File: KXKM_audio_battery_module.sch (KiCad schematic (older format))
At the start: 22 parts, among them J1 Conn_01x06, J2 TEST_1P, J3 mikroBUS_socket, J4 Conn_01x04, J5 Micro_SD_Card, J6 Conn_01x03, J7 Conn_01x04, Q1 DMN63D8LDW, Q2 DMN63D8LDW, SW1 SW_Push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

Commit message: Component placement WIP - multiple Hammond enclosures drawn
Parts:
- RN1, RN2, RN3: footprint (none) -> Resistors_SMD:R_Array_Convex_4x0402
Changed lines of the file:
@@
 F 0 "RN1" H 2130 4470 50  0000 L CNN
 F 1 "10k" H 2130 4410 50  0000 L CNN
-F 2 "" H 2100 4450 50  0001 C CNN
+F 2 "Resistors_SMD:R_Array_Convex_4x0402" H 2100 4450 50  0001 C CNN
 F 3 "" H 2100 4450 50  0001 C CNN
 	3    2100 4450
@@
 F 0 "RN1" H 2030 4470 50  0000 L CNN
 F 1 "10k" H 2030 4410 50  0000 L CNN
-F 2 "" H 2000 4450 50  0001 C CNN
+F 2 "Resistors_SMD:R_Array_Convex_4x0402" H 2000 4450 50  0001 C CNN
 F 3 "" H 2000 4450 50  0001 C CNN
 	2    2000 4450
@@
 F 0 "RN1" H 3480 1870 50  0000 L CNN
 F 1 "10k" H 3480 1810 50  0000 L CNN
-F 2 "" H 3450 1850 50  0001 C CNN
+F 2 "Resistors_SMD:R_Array_Convex_4x0402" H 3450 1850 50  0001 C CNN
 F 3 "" H 3450 1850 50  0001 C CNN
 	4    3450 1850
@@
 F 0 "RN3" H 9830 5220 50  0000 L CNN
 F 1 "10k" H 9830 5160 50  0000 L CNN
-F 2 "" H 9800 5200 50  0001 C CNN
+F 2 "Resistors_SMD:R_Array_Convex_4x0402" H 9800 5200 50  0001 C CNN
 F 3 "" H 9800 5200 50  0001 C CNN
 	1    9800 5200
@@
 F 0 "RN3" H 9830 5870 50  0000 L CNN
 F 1 "10k" H 9830 5810 50  0000 L CNN
-F 2 "" H 9800 5850 50  0001 C CNN
+F 2 "Resistors_SMD:R_Array_Convex_4x0402" H 9800 5850 50  0001 C CNN
 F 3 "" H 9800 5850 50  0001 C CNN
 	2    9800 5850
@@
 F 0 "RN2" H 8930 5870 50  0000 L CNN
 F 1 "10k" H 8930 5810 50  0000 L CNN
-F 2 "" H 8900 5850 50  0001 C CNN
+F 2 "Resistors_SMD:R_Array_Convex_4x0402" H 8900 5850 50  0001 C CNN
 F 3 "" H 8900 5850 50  0001 C CNN
 	4    8900 5850
@@
 F 0 "RN2" H 8930 5220 50  0000 L CNN
 F 1 "10k" H 8930 5160 50  0000 L CNN
-F 2 "" H 8900 5200 50  0001 C CNN
+F 2 "Resistors_SMD:R_Array_Convex_4x0402" H 8900 5200 50  0001 C CNN
 F 3 "" H 8900 5200 50  0001 C CNN
 	3    8900 5200
@@
 F 0 "RN1" V 1850 6850 50  0000 L CNN
 F 1 "10k" V 1850 7150 50  0000 L CNN
-F 2 "" H 1900 7050 50  0001 C CNN
+F 2 "Resistors_SMD:R_Array_Convex_4x0402" H 1900 7050 50  0001 C CNN
 F 3 "" H 1900 7050 50  0001 C CNN
 	1    1900 7050
@@
 F 0 "RN2" V 3450 7150 50  0000 L CNN
 F 1 "10k" V 3650 7150 50  0000 L CNN
-F 2 "" H 3550 7250 50  0001 C CNN
+F 2 "Resistors_SMD:R_Array_Convex_4x0402" H 3550 7250 50  0001 C CNN
 F 3 "" H 3550 7250 50  0001 C CNN
 	2    3550 7250
@@
 F 0 "RN2" V 3450 6650 50  0000 L CNN
 F 1 "10k" V 3650 6650 50  0000 L CNN
-F 2 "" H 3550 6750 50  0001 C CNN
+F 2 "Resistors_SMD:R_Array_Convex_4x0402" H 3550 6750 50  0001 C CNN
 F 3 "" H 3550 6750 50  0001 C CNN
 	1    3550 6750

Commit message: Almost all components placed... Saving before mirroring everything
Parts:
- J2: footprint Connectors_TestPoints:Test_Point_Pad_d2.0mm -> Connectors_TestPoints:Test_Point_Pad_d1.5mm
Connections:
- net +5V: no longer J7.1 (Pin_1), RN3.1, RN3.2
- new net VBUS: J7.1 (Pin_1), RN3.1, RN3.2
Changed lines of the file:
@@
-	1    0    0    -1
-$EndComp
-$Comp
-L +5V #PWR016
-U 1 1 5AA2789C
-P 10600 5500
-F 0 "#PWR016" H 10600 5350 50  0001 C CNN
-F 1 "+5V" H 10600 5640 50  0000 C CNN
-F 2 "" H 10600 5500 50  0001 C CNN
-F 3 "" H 10600 5500 50  0001 C CNN
-	1    10600 5500
 	1    0    0    -1
 $EndComp
@@
 I2C_SDA
 $Comp
-L GND #PWR017
+L GND #PWR016
 U 1 1 5AA0EF07
 P 6300 6600
-F 0 "#PWR017" H 6300 6350 50  0001 C CNN
+F 0 "#PWR016" H 6300 6350 50  0001 C CNN
 F 1 "GND" H 6300 6450 50  0000 C CNN
 F 2 "" H 6300 6600 50  0001 C CNN
@@
 $EndComp
 $Comp
-L +3.3V #PWR018
+L +3.3V #PWR017
 U 1 1 5AA0F052
 P 6100 6750
-F 0 "#PWR018" H 6100 6600 50  0001 C CNN
+F 0 "#PWR017" H 6100 6600 50  0001 C CNN
 F 1 "+3.3V" H 6100 6890 50  0000 C CNN
 F 2 "" H 6100 6750 50  0001 C CNN
@@
 F 0 "J2" H 1750 2720 50  0000 C CNN
 F 1 "TEST_1P" H 1750 2650 50  0000 C CNN
-F 2 "Connectors_TestPoints:Test_Point_Pad_d2.0mm" H 1950 2450 50  0001 C CNN
+F 2 "Connectors_TestPoints:Test_Point_Pad_d1.5mm" H 1950 2450 50  0001 C CNN
 F 3 "" H 1950 2450 50  0001 C CNN
 	1    1750 2450
@@
 	1550 2550 1750 2550
 $Comp
-L GND #PWR019
+L GND #PWR018
 U 1 1 5AA165C1
 P 2200 2550
-F 0 "#PWR019" H 2200 2300 50  0001 C CNN
+F 0 "#PWR018" H 2200 2300 50  0001 C CNN
 F 1 "GND" H 2200 2400 50  0000 C CNN
 F 2 "" H 2200 2550 50  0001 C CNN
@@
 Serial & programmation connector with ESP32 auto-reset
 $Comp
-L GND #PWR020
+L GND #PWR019
 U 1 1 5AA19B5E
 P 2400 6700
-F 0 "#PWR020" H 2400 6450 50  0001 C CNN
+F 0 "#PWR019" H 2400 6450 50  0001 C CNN
 F 1 "GND" H 2400 6550 50  0000 C CNN
 F 2 "" H 2400 6700 50  0001 C CNN
@@
 PROG_RTS
 $Comp
-L +3.3V #PWR021
+L +3.3V #PWR020
 U 1 1 5AA19EC3
 P 2600 6900
-F 0 "#PWR021" H 2600 6750 50  0001 C CNN
+F 0 "#PWR020" H 2600 6750 50  0001 C CNN
 F 1 "+3.3V" H 2600 7040 50  0000 C CNN
 F 2 "" H 2600 6900 50  0001 C CNN
@@
 $EndComp
 $Comp
-L GND #PWR022
+L GND #PWR021
 U 1 1 5AA1B90F
 P 3800 2600
-F 0 "#PWR022" H 3800 2350 50  0001 C CNN
+F 0 "#PWR021" H 3800 2350 50  0001 C CNN
 F 1 "GND" H 3800 2450 50  0000 C CNN
 F 2 "" H 3800 2600 50  0001 C CNN
@@
 Connection ~ 9800 6000
 $Comp
-L +3.3V #PWR023
+L +3.3V #PWR022
 U 1 1 5AA2C62F
 P 8900 5600
-F 0 "#PWR023" H 8900 5450 50  0001 C CNN
+F 0 "#PWR022" H 8900 5450 50  0001 C CNN
 F 1 "+3.3V" H 8900 5740 50  0000 C CNN
 F 2 "" H 8900 5600 50  0001 C CNN
@@
 	9100 5000 9100 5050
 Connection ~ 8900 5000
-$Comp
-L +5V #PWR024
-U 1 1 5AA2D14C
-P 9800 4950
-F 0 "#PWR024" H 9800 4800 50  0001 C CNN
-F 1 "+5V" H 9800 5090 50  0000 C CNN
-F 2 "" H 9800 4950 50  0001 C CNN
-F 3 "" H 9800 4950 50  0001 C CNN
-	1    9800 4950
-	1    0    0    -1
-$EndComp
 Wire Wire Line
 	9800 4950 9800 5100
-$Comp
-L +5V #PWR025
-U 1 1 5AA2D30B
-P 9800 5600
-F 0 "#PWR025" H 9800 5450 50  0001 C CNN
-F 1 "+5V" H 9800 5740 50  0000 C CNN
-F 2 "" H 9800 5600 50  0001 C CNN
-F 3 "" H 9800 5600 50  0001 C CNN
-	1    9800 5600
-	1    0    0    -1
-$EndComp
 Wire Wire Line
 	9800 5750 9800 5600
 $Comp
-L +3.3V #PWR026
+L +3.3V #PWR023
 U 1 1 5AA2F1DB
 P 1500 5000
-F 0 "#PWR026" H 1500 4850 50  0001 C CNN
+F 0 "#PWR023" H 1500 4850 50  0001 C CNN
 F 1 "+3.3V" H 1500 5140 50  0000 C CNN
 F 2 "" H 1500 5000 50  0001 C CNN
@@
 	7150 5700 7850 5700
 $Comp
-L GND #PWR027
+L GND #PWR024
 U 1 1 5AA3BD4C
 P 5700 5950
-F 0 "#PWR027" H 5700 5700 50  0001 C CNN
+F 0 "#PWR024" H 5700 5700 50  0001 C CNN
 F 1 "GND" H 5700 5800 50  0000 C CNN
 F 2 "" H 5700 5950 50  0001 C CNN
@@
 $EndComp
 $Comp
-L GND #PWR028
+L GND #PWR025
 U 1 1 5AA3BE20
 P 7200 5950
-F 0 "#PWR028" H 7200 5700 50  0001 C CNN
+F 0 "#PWR025" H 7200 5700 50  0001 C CNN
 F 1 "GND" H 7200 5800 50  0000 C CNN
 F 2 "" H 7200 5950 50  0001 C CNN
@@
 	7200 5900 7200 5950
 $Comp
-L +3.3V #PWR029
+L +3.3V #PWR026
 U 1 1 5AA3C3D7
 P 5500 5950
-F 0 "#PWR029" H 5500 5800 50  0001 C CNN
+F 0 "#PWR026" H 5500 5800 50  0001 C CNN
 F 1 "+3.3V" H 5500 6090 50  0000 C CNN
 F 2 "" H 5500 5950 50  0001 C CNN
@@
 	5650 5800 5750 5800
 $Comp
-L +5V #PWR030
+L +5V #PWR027
 U 1 1 5AA3C5B1
 P 7400 5950
-F 0 "#PWR030" H 7400 5800 50  0001 C CNN
+F 0 "#PWR027" H 7400 5800 50  0001 C CNN
 F 1 "+5V" H 7400 6090 50  0000 C CNN
 F 2 "" H 7400 5950 50  0001 C CNN
@@
 	2750 5550 2750 5500
 $Comp
-L GND #PWR031
+L GND #PWR028
 U 1 1 5AA26AF5
 P 2750 5550
-F 0 "#PWR031" H 2750 5300 50  0001 C CNN
+F 0 "#PWR028" H 2750 5300 50  0001 C CNN
 F 1 "GND" H 2750 5400 50  0000 C CNN
 F 2 "" H 2750 5550 50  0001 C CNN
@@
 	6200 3600 6200 3850
 $Comp
-L GND #PWR032
+L GND #PWR029
 U 1 1 5AA26E5F
 P 6500 1250
-F 0 "#PWR032" H 6500 1000 50  0001 C CNN
+F 0 "#PWR029" H 6500 1000 50  0001 C CNN
 F 1 "GND" H 6500 1100 50  0000 C CNN
 F 2 "" H 6500 1250 50  0001 C CNN
@@
 	3400 6800 3400 6750
 Connection ~ 3400 6750
+$Comp
+L VBUS #PWR030
+U 1 1 5AA7F3B8
+P 9800 4950
+F 0 "#PWR030" H 9800 4800 50  0001 C CNN
+F 1 "VBUS" H 9800 5100 50  0000 C CNN
+F 2 "" H 9800 4950 50  0001 C CNN
+F 3 "" H 9800 4950 50  0001 C CNN
+	1    9800 4950
+	1    0    0    -1
+$EndComp
+$Comp
+L VBUS #PWR031
+U 1 1 5AA7F756
+P 9800 5600
+F 0 "#PWR031" H 9800 5450 50  0001 C CNN
+F 1 "VBUS" H 9800 5750 50  0000 C CNN
+F 2 "" H 9800 5600 50  0001 C CNN
+F 3 "" H 9800 5600 50  0001 C CNN
+	1    9800 5600
+	1    0    0    -1
+$EndComp
+$Comp
+L VBUS #PWR032
+U 1 1 5AA7FB52
+P 10600 5500
+F 0 "#PWR032" H 10600 5350 50  0001 C CNN
+F 1 "VBUS" H 10600 5650 50  0000 C CNN
+F 2 "" H 10600 5500 50  0001 C CNN
+F 3 "" H 10600 5500 50  0001 C CNN
+	1    10600 5500
+	1    0    0    -1
+$EndComp
 $EndSCHEMATC

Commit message: v1.0   Add 3D files with Hammond enclosures  fabrication outputs
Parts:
- added Q3: DMN63D8LDW, TO_SOT_Packages_SMD:SOT-363_SC-70-6, symbol FDG1024NZ
- added R2: 10k, Resistors_SMD:R_0603, symbol R_Small
- J4: footprint Socket_Strips:Socket_Strip_Straight_1x04_Pitch2.54mm -> Pin_Headers:Pin_Header_Straight_1x04_Pitch2.54mm_SMD_Pin1Left
- renumbered RN1 to RN2, RN2 to RN3
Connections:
- net +3V3: now also RN1.1, RN3.3, RN3.4, Q3.5 (G), R2.1; no longer RN1.3, RN3.3, RN3.4
- net Battery monitoring/ESP32_EN: now also RN1.3; no longer RN1.4
- net DMX_DE: now also J3.2 (RST), U1.9 (IO33); no longer J3.15 (INT), U1.12 (IO27)
- net DMX_DI: now also U1.8 (IO32); no longer U1.24 (IO2)
- net ESP32_BOOT: now also Q3.4 (S)
- net ESP32_EN: now also RN1.6; no longer RN1.5
- net ESP32_RXI: now also RN2.6; no longer RN2.1
- net GP_PUSH_BTN: now also R2.2
- net I2C_SCL: now also RN1.8, U1.26 (IO4); no longer RN1.6, U1.9 (IO33)
- net I2C_SDA: now also U1.24 (IO2), Q3.3 (D); no longer U1.8 (IO32)
- net I2S_BCK: now also U1.10 (IO25); no longer U1.11 (IO26)
- net I2S_DATA: now also U1.11 (IO26); no longer U1.36 (IO22)
- net I2S_LRCK: now also U1.12 (IO27); no longer U1.10 (IO25)
- net LED_DATA_1: now also J3.15 (INT), RN3.6; no longer J3.2 (RST), RN3.6
- net LED_DATA_2: now also RN3.5, U1.36 (IO22); no longer RN3.5, U1.26 (IO4)
- net PROG_DTR: now also RN2.2; no longer RN2.7
- net PROG_RTS: now also RN2.1; no longer RN2.8
- net at J1.4 (Pin_4): now also RN2.3; no longer RN2.8
- net at Q1.2 (G): now also RN2.8; no longer RN2.1
- net at Q1.5 (G): now also RN2.7; no longer RN2.2
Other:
- note added: "DTR RTS => EN IO0&IO2\n 1 1 1 1\n 0 0 1 1\n 1 0 0 1\n 0 1 1 0"
- note added: "General purpose push button"
- note added: "IO0 and IO2 are pulled Low \nwhen DTR = 0 and RTS = 1.\nOtherwise they are floating.\nIO0 has an internal PU."
- note added: "Input only\nNo PU, no PD"
- note added: "NB : IO15 = MTDO = debug log enabled\nIO0 AND IO2 must be low to enter BL \nIO2 : internal PD, IO0 : internal PU"
- note added: "ToDo : need pull up on IO0 !?"
- note removed: "Input only !"
- note removed: "NB : IO15 = MTDO = debug log enabled\nIO2 must be low to enter BL (internal PD)"
- note removed: "ToDO : resistor arrays\n"
- moved on the sheet: J1, Q1A, Q1B, RN2A, RN2B, SW2

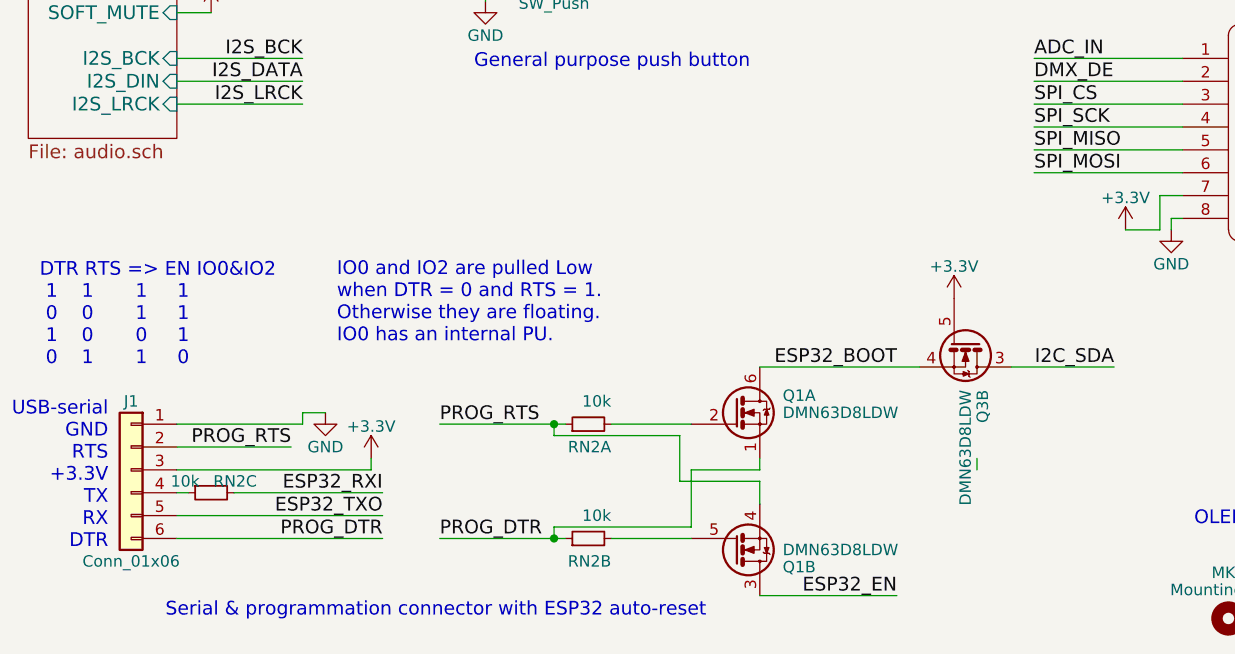
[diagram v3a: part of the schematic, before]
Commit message: v1.1 - changed some resistor values ; manufacturability improvements (thermal relief) ; added a test point for ESP32_EN
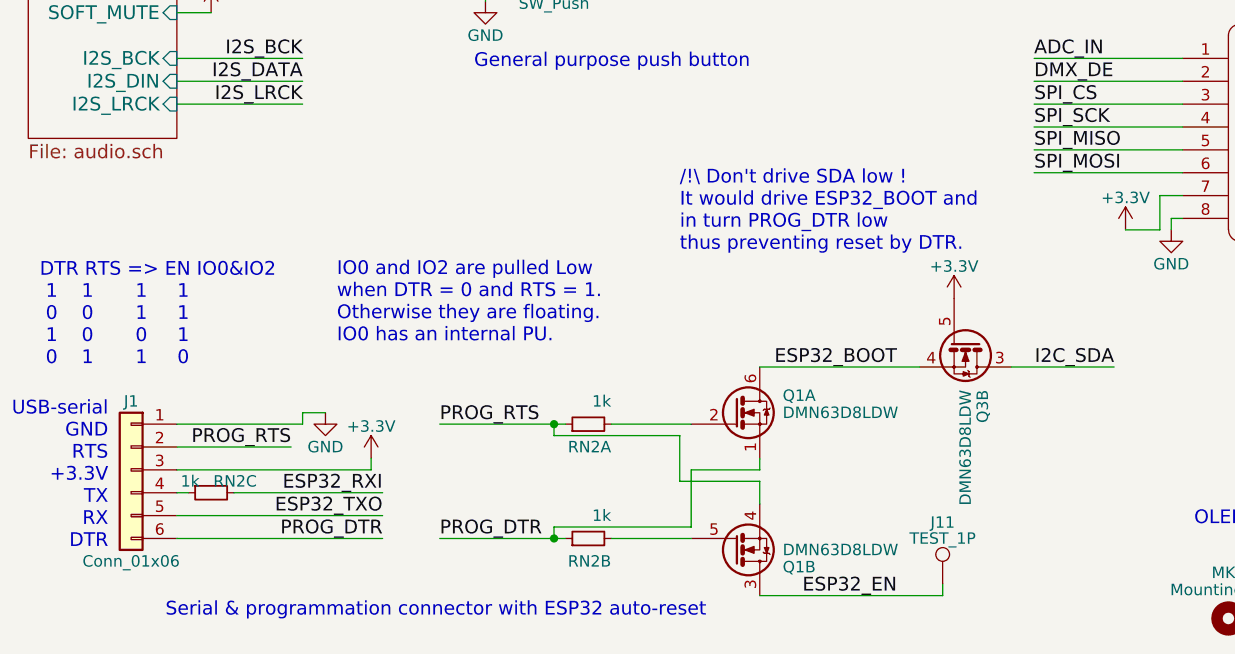
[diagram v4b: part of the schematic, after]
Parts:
- added J11: TEST_1P, Connectors_TestPoints:Test_Point_Pad_d1.5mm, symbol TEST_1P
- RN2: value 10k -> 1k
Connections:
- net ESP32_EN: now also J11.1
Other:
- note added: "/!\ Don't drive SDA low ! \nIt would drive ESP32_BOOT and \nin turn PROG_DTR low \nthus preventing reset by DTR."
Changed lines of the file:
@@
 Sheet 1 4
 Title "ESP32 Audio & Battery module"
-Date "2018-03-15"
-Rev "1.0"
+Date "2018-03-29"
+Rev "1.1"
 Comp "KXKM"
 Comment1 "Tom Magnier"
@@
 P 1500 7100
 F 0 "RN2" V 1450 6900 50  0000 L CNN
-F 1 "10k" V 1450 7150 50  0000 L CNN
+F 1 "1k" V 1450 7150 50  0000 L CNN
 F 2 "Resistors_SMD:R_Array_Convex_4x0402" H 1500 7100 50  0001 C CNN
 F 3 "" H 1500 7100 50  0001 C CNN
@@
 P 3150 7300
 F 0 "RN2" V 3050 7200 50  0000 L CNN
-F 1 "10k" V 3250 7200 50  0000 L CNN
+F 1 "1k" V 3250 7200 50  0000 L CNN
 F 2 "Resistors_SMD:R_Array_Convex_4x0402" H 3150 7300 50  0001 C CNN
 F 3 "" H 3150 7300 50  0001 C CNN
@@
 P 3150 6800
 F 0 "RN2" V 3050 6700 50  0000 L CNN
-F 1 "10k" V 3250 6700 50  0000 L CNN
+F 1 "1k" V 3250 6700 50  0000 L CNN
 F 2 "Resistors_SMD:R_Array_Convex_4x0402" H 3150 6800 50  0001 C CNN
 F 3 "" H 3150 6800 50  0001 C CNN
@@
 Wire Wire Line
 	5000 6550 5450 6550
-Wire Wire Line
-	4850 6950 4850 7000
 Connection ~ 3000 6800
 Wire Wire Line
@@
 	3600 7250 3000 7250
 Wire Wire Line
-	3900 7550 4500 7550
+	3900 7550 4700 7550
 Wire Wire Line
 	3250 7300 3600 7300
@@
 	1    0    0    -1
 $EndComp
+Text Notes 3550 6050 0    60   ~ 0
+/!\ Don't drive SDA low ! \nIt would drive ESP32_BOOT and \nin turn PROG_DTR low \nthus preventing reset by DTR.
+$Comp
+L TEST_1P J11
+U 1 1 5ABD450A
+P 4700 7500
+F 0 "J11" H 4700 7770 50  0000 C CNN
+F 1 "TEST_1P" H 4700 7700 50  0000 C CNN
+F 2 "Connectors_TestPoints:Test_Point_Pad_d1.5mm" H 4900 7500 50  0001 C CNN
+F 3 "" H 4900 7500 50  0001 C CNN
+	1    4700 7500
+	1    0    0    -1
+$EndComp
+Wire Wire Line
+	4700 7550 4700 7500
 $EndSCHEMATC

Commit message: Update BOM & fab files
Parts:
- R2: value 10k -> 10k,1%
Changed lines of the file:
@@
 P 3300 4650
 F 0 "R2" H 3330 4670 50  0000 L CNN
-F 1 "10k" H 3330 4610 50  0000 L CNN
+F 1 "10k,1%" H 3330 4610 50  0000 L CNN
 F 2 "Resistors_SMD:R_0603" H 3300 4650 50  0001 C CNN
 F 3 "" H 3300 4650 50  0001 C CNN
